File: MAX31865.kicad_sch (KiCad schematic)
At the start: 22 parts, among them J1 connector, J2 Screw_Terminal_01x04, U1 MAX31865, U2 MIC5225

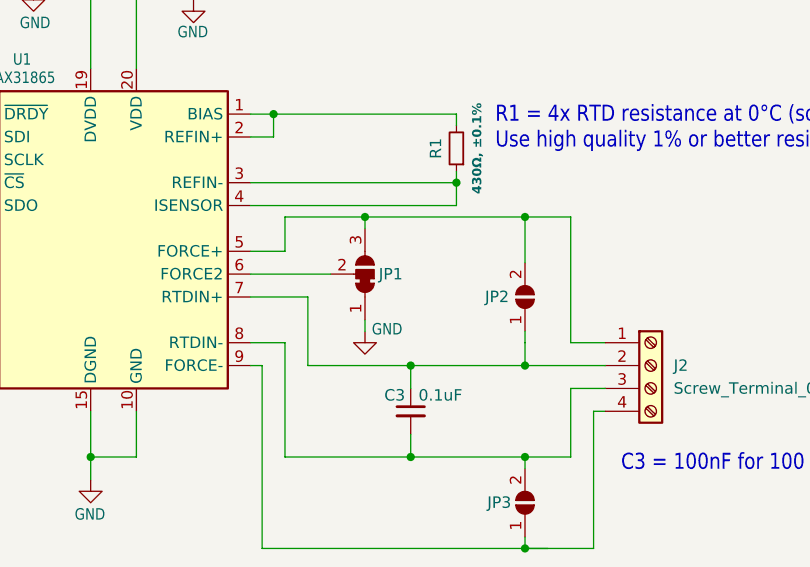
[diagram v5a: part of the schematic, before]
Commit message: schematic update
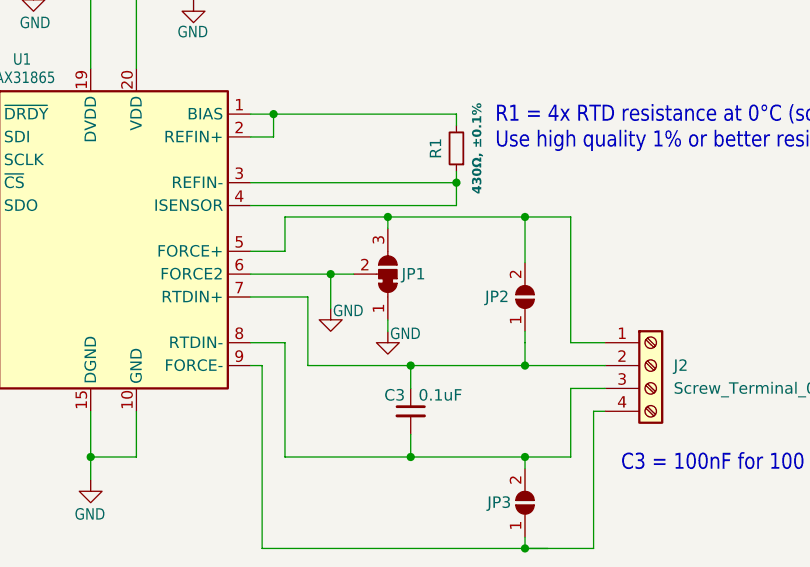
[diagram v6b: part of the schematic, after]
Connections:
- net GND: now also JP1.2 (C), U1.6 (FORCE2)
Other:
- moved on the sheet: JP1
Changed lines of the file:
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@@
 	)
 	(junction
+		(at 153.67 99.06)
+		(diameter 0)
+		(color 0 0 0 0)
+	)
+	(junction
 		(at 175.26 119.38)
 		(diameter 0)
@@
 	)
 	(junction
-		(at 157.48 92.71)
+		(at 127 119.38)
 		(diameter 0)
 		(color 0 0 0 0)
 	)
 	(junction
-		(at 127 119.38)
+		(at 68.58 113.03)
 		(diameter 0)
 		(color 0 0 0 0)
 	)
 	(junction
-		(at 68.58 113.03)
+		(at 160.02 92.71)
 		(diameter 0)
 		(color 0 0 0 0)
@@
 	(wire
 		(pts
-			(xy 157.48 92.71) (xy 175.26 92.71)
-		)
-		(stroke
-			(width 0.1524)
-			(type solid)
-		)
-	)
-	(wire
-		(pts
 			(xy 132.08 59.69) (xy 132.08 76.2)
 		)
@@
 	(wire
 		(pts
-			(xy 148.59 92.71) (xy 157.48 92.71)
+			(xy 148.59 92.71) (xy 160.02 92.71)
 		)
 		(stroke
@@
 	(wire
 		(pts
+			(xy 153.67 99.06) (xy 156.21 99.06)
+		)
+		(stroke
+			(width 0.1524)
+			(type solid)
+		)
+	)
+	(wire
+		(pts
 			(xy 175.26 109.22) (xy 184.15 109.22)
 		)
@@
 	(wire
 		(pts
-			(xy 157.48 92.71) (xy 157.48 93.98)
+			(xy 160.02 92.71) (xy 160.02 93.98)
 		)
 		(stroke
@@
 	(wire
 		(pts
+			(xy 160.02 92.71) (xy 175.26 92.71)
+		)
+		(stroke
+			(width 0.1524)
+			(type solid)
+		)
+	)
+	(wire
+		(pts
 			(xy 114.3 86.36) (xy 91.44 86.36)
 		)
@@
 	(wire
 		(pts
+			(xy 153.67 99.06) (xy 153.67 102.87)
+		)
+		(stroke
+			(width 0)
+			(type default)
+		)
+	)
+	(wire
+		(pts
 			(xy 138.43 67.31) (xy 138.43 68.58)
 		)
@@
 	(wire
 		(pts
-			(xy 157.48 105.41) (xy 157.48 104.14)
+			(xy 160.02 105.41) (xy 160.02 104.14)
 		)
 		(stroke
@@
 	(symbol
 		(lib_id "power:GND")
+		(at 153.67 102.87 0)
+		(unit 1)
+		(exclude_from_sim no)
+		(in_bom yes)
+		(on_board yes)
+		(dnp no)
+		(property "Reference" "#U$08"
+			(at 153.67 102.87 0)
+			(effects
+				(font
+					(size 1.27 1.27)
+				)
+				(hide yes)
+			)
+		)
+		(property "Value" "GND"
+			(at 153.924 103.886 0)
+			(effects
+				(font
+					(size 1.27 1.0795)
+				)
+				(justify left bottom)
+			)
+		)
+		(property "Footprint" ""
+			(at 153.67 102.87 0)
+			(effects
+				(font
+					(size 1.27 1.27)
+				)
+				(hide yes)
+			)
+		)
+		(property "Datasheet" ""
+			(at 153.67 102.87 0)
+			(effects
+				(font
+					(size 1.27 1.27)
+				)
+				(hide yes)
+			)
+		)
+		(property "Description" "Power symbol creates a global label with name \"GND\" , ground"
+			(at 153.67 102.87 0)
+			(effects
+				(font
+					(size 1.27 1.27)
+				)
+				(hide yes)
+			)
+		)
+		(pin "1"
+		)
+		(instances
+			(project "MAX31865"
+				(path "/7d3dfe06-ad22-4135-8721-3b06d69e4560"
+					(reference "#U$08")
+					(unit 1)
+				)
+			)
+		)
+	)
+	(symbol
+		(lib_id "power:GND")
 		(at 91.44 130.81 0)
 		(unit 1)
@@
 	(symbol
 		(lib_id "power:GND")
-		(at 157.48 105.41 0)
+		(at 160.02 105.41 0)
 		(unit 1)
 		(exclude_from_sim no)
@@
 		(dnp no)
 		(property "Reference" "#U$06"
-			(at 157.48 105.41 0)
+			(at 160.02 105.41 0)
 			(effects
 				(font
@@
 		)
 		(property "Value" "GND"
-			(at 158.242 105.918 0)
+			(at 160.274 106.426 0)
 			(effects
 				(font
@@
 		)
 		(property "Footprint" ""
-			(at 157.48 105.41 0)
+			(at 160.02 105.41 0)
 			(effects
 				(font
@@
 		)
 		(property "Datasheet" ""
-			(at 157.48 105.41 0)
+			(at 160.02 105.41 0)
 			(effects
 				(font
@@
 		)
 		(property "Description" "Power symbol creates a global label with name \"GND\" , ground"
-			(at 157.48 105.41 0)
+			(at 160.02 105.41 0)
 			(effects
 				(font
@@
 	(symbol
 		(lib_id "Jumper:SolderJumper_3_Bridged12")
-		(at 157.48 99.06 270)
+		(at 160.02 99.06 270)
 		(mirror x)
 		(unit 1)
@@
 		(dnp no)
 		(property "Reference" "JP1"
-			(at 159.004 99.06 90)
+			(at 161.544 99.06 90)
 			(effects
 				(font
@@
 		)
 		(property "Value" "SolderJumper_3_Bridged12"
-			(at 160.02 97.7901 90)
+			(at 162.56 97.7901 90)
 			(effects
 				(font
@@
 		)
 		(property "Footprint" "Jumper:SolderJumper-3_P1.3mm_Bridged12_Pad1.0x1.5mm"
-			(at 157.48 99.06 0)
+			(at 160.02 99.06 0)
 			(effects
 				(font
@@
 		)
 		(property "Datasheet" "~"
-			(at 157.48 99.06 0)
+			(at 160.02 99.06 0)
 			(effects
 				(font
@@
 		)
 		(property "Description" "3-pole Solder Jumper, pins 1+2 closed/bridged"
-			(at 157.48 99.06 0)
+			(at 160.02 99.06 0)
 			(effects
 				(font

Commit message: implemented Eurocircuits design remarks
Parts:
- FB1: footprint Inductor_SMD:L_0805_2012Metric -> external_footprints:LI0805G201R-10
- J2: MPN 0393570004 -> 039357-0004
- U1: footprint Package_DFN_QFN:TQFN-20-1EP_5x5mm_P0.65mm_EP3.25x3.25mm -> external_footprints:MAX31865ATP+
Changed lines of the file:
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@@
 			)
 		)
-		(property "Datasheet" "~"
+		(property "Datasheet" ""
 			(at 91.44 123.19 0)
 			(effects
@@
 			)
 		)
-		(property "Datasheet" "~"
+		(property "Datasheet" ""
 			(at 175.26 124.46 0)
 			(effects
@@
 			)
 		)
-		(property "Datasheet" "~"
+		(property "Datasheet" ""
 			(at 175.26 101.6 0)
 			(effects
@@
 			)
 		)
-		(property "Datasheet" "~"
+		(property "Datasheet" ""
 			(at 99.06 76.2 0)
 			(effects
@@
 			)
 		)
-		(property "Datasheet" "~"
+		(property "Datasheet" ""
 			(at 60.96 52.07 0)
 			(effects
@@
 			)
 		)
-		(property "Footprint" "Package_DFN_QFN:TQFN-20-1EP_5x5mm_P0.65mm_EP3.25x3.25mm"
+		(property "Footprint" "external_footprints:MAX31865ATP+"
 			(at 133.35 113.03 0)
 			(effects
@@
 			)
 		)
-		(property "Datasheet" "https://datasheets.maximintegrated.com/en/ds/MAX31865.pdf"
+		(property "Datasheet" ""
 			(at 129.54 88.9 0)
 			(effects
@@
 			)
 		)
-		(property "Datasheet" "~"
+		(property "Datasheet" ""
 			(at 73.66 90.17 0)
 			(effects
@@
 			)
 		)
-		(property "Datasheet" "~"
+		(property "Datasheet" ""
 			(at 167.64 85.09 0)
 			(effects
@@
 			)
 		)
-		(property "Datasheet" "~"
+		(property "Datasheet" ""
 			(at 138.43 64.77 0)
 			(effects
@@
 			)
 		)
-		(property "Footprint" "Inductor_SMD:L_0805_2012Metric"
+		(property "Footprint" "external_footprints:LI0805G201R-10"
 			(at 133.858 55.88 90)
 			(effects
@@
 			)
 		)
-		(property "Datasheet" "~"
+		(property "Datasheet" ""
 			(at 132.08 55.88 0)
 			(effects
@@
 			)
 		)
-		(property "Datasheet" "~"
+		(property "Datasheet" ""
 			(at 162.56 114.3 0)
 			(effects
@@
 			)
 		)
-		(property "Datasheet" "~"
+		(property "Datasheet" ""
 			(at 134.62 157.48 0)
 			(effects
@@
 			)
 		)
-		(property "Datasheet" "~"
+		(property "Datasheet" ""
 			(at 120.65 63.5 0)
 			(effects
@@
 			)
 		)
-		(property "Datasheet" "~"
+		(property "Datasheet" ""
 			(at 189.23 109.22 0)
 			(effects
@@
 			)
 		)
-		(property "MPN" "0393570004"
+		(property "MPN" "039357-0004"
 			(at 189.23 109.22 0)
 			(effects
@@
 			)
 		)
-		(property "Datasheet" "~"
+		(property "Datasheet" ""
 			(at 53.34 52.07 0)
 			(effects
@@
 			)
 		)
-		(property "Datasheet" "~"
+		(property "Datasheet" ""
 			(at 95.25 69.85 0)
 			(effects
@@
 			)
 		)
-		(property "Datasheet" "~"
+		(property "Datasheet" ""
 			(at 63.5 120.65 0)
 			(effects
@@
 			)
 		)
-		(property "Datasheet" "~"
+		(property "Datasheet" ""
 			(at 160.02 99.06 0)
 			(effects
@@
 			)
 		)
-		(property "Datasheet" "~"
+		(property "Datasheet" ""
 			(at 91.44 76.2 0)
 			(effects
@@
 			)
 		)
-		(property "Datasheet" "~"
+		(property "Datasheet" ""
 			(at 73.66 86.36 0)
 			(effects

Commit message: BOM presets update
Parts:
- C4, C5: Component package type C_0805 -> (none)
- D1, D2, D3: Component package type SOD-323 -> (none)
- J1: Component package type / -> (none)
- U1: Component package type 20-TQFN (5x5) -> (none)
- U2: Component package type SOT-235 -> (none)
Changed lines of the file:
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@@
 			)
 		)
-		(property "Component package type" "SOT-235"
-			(at 73.66 119.38 0)
-			(effects
-				(font
-					(size 1.27 1.27)
-				)
-				(hide yes)
-			)
-		)
 		(property "MPN" "MIC5225-3.3YM5-TR"
 			(at 73.66 119.38 0)
@@
 			)
 		)
-		(property "Component package type" "C_0805"
-			(at 91.44 123.19 0)
-			(effects
-				(font
-					(size 1.27 1.27)
-				)
-				(hide yes)
-			)
-		)
 		(property "MPN" "/"
 			(at 91.44 123.19 0)
@@
 			)
 		)
-		(property "Component package type" ""
-			(at 175.26 124.46 0)
-			(effects
-				(font
-					(size 1.27 1.27)
-				)
-				(hide yes)
-			)
-		)
 		(property "MPN" ""
 			(at 175.26 124.46 0)
@@
 			)
 		)
-		(property "Component package type" ""
-			(at 175.26 101.6 0)
-			(effects
-				(font
-					(size 1.27 1.27)
-				)
-				(hide yes)
-			)
-		)
 		(property "MPN" ""
 			(at 175.26 101.6 0)
@@
 			)
 		)
-		(property "Component package type" ""
-			(at 99.06 76.2 0)
-			(effects
-				(font
-					(size 1.27 1.27)
-				)
-				(hide yes)
-			)
-		)
 		(property "MPN" "/"
 			(at 99.06 76.2 0)
@@
 			)
 		)
-		(property "Component package type" ""
-			(at 60.96 52.07 0)
-			(effects
-				(font
-					(size 1.27 1.27)
-				)
-				(hide yes)
-			)
-		)
 		(property "MPN" ""
 			(at 60.96 52.07 0)
@@
 			)
 		)
-		(property "Component package type" "20-TQFN (5x5)"
-			(at 129.54 96.52 0)
-			(effects
-				(font
-					(size 1.27 1.27)
-				)
-				(hide yes)
-			)
-		)
 		(property "MPN" "MAX31865ATP+"
 			(at 129.54 96.52 0)
@@
 			)
 		)
-		(property "Component package type" "SOD-323"
-			(at 73.66 90.17 0)
-			(effects
-				(font
-					(size 1.27 1.27)
-				)
-				(hide yes)
-			)
-		)
 		(property "MPN" "1N4148WX-TP"
 			(at 73.66 90.17 0)
@@
 			)
 		)
-		(property "Component package type" ""
-			(at 167.64 85.09 0)
-			(effects
-				(font
-					(size 1.27 1.27)
-				)
-				(hide yes)
-			)
-		)
 		(property "MPN" "/"
 			(at 167.64 85.09 0)
@@
 			)
 		)
-		(property "Component package type" ""
-			(at 138.43 64.77 0)
-			(effects
-				(font
-					(size 1.27 1.27)
-				)
-				(hide yes)
-			)
-		)
 		(property "MPN" "/"
 			(at 138.43 64.77 0)
@@
 			)
 		)
-		(property "Component package type" ""
-			(at 132.08 55.88 0)
-			(effects
-				(font
-					(size 1.27 1.27)
-				)
-				(hide yes)
-			)
-		)
 		(property "MPN" "LI0805G201R-10"
 			(at 132.08 55.88 0)
@@
 			)
 		)
-		(property "Component package type" ""
-			(at 162.56 114.3 0)
-			(effects
-				(font
-					(size 1.27 1.27)
-				)
-				(hide yes)
-			)
-		)
 		(property "MPN" "/"
 			(at 162.56 114.3 0)
@@
 			)
 		)
-		(property "Component package type" "/"
-			(at 134.62 157.48 0)
-			(effects
-				(font
-					(size 1.27 1.27)
-				)
-				(hide yes)
-			)
-		)
 		(property "MPN" "TSW-108-09-G-S"
 			(at 134.62 157.48 0)
@@
 			)
 		)
-		(property "Component package type" ""
-			(at 120.65 63.5 0)
-			(effects
-				(font
-					(size 1.27 1.27)
-				)
-				(hide yes)
-			)
-		)
 		(property "MPN" "/"
 			(at 120.65 63.5 0)
@@
 			)
 		)
-		(property "Component package type" ""
-			(at 53.34 52.07 0)
-			(effects
-				(font
-					(size 1.27 1.27)
-				)
-				(hide yes)
-			)
-		)
 		(property "MPN" ""
 			(at 53.34 52.07 0)
@@
 			)
 		)
-		(property "Component package type" ""
-			(at 95.25 69.85 0)
-			(effects
-				(font
-					(size 1.27 1.27)
-				)
-				(hide yes)
-			)
-		)
 		(property "MPN" "/"
 			(at 95.25 69.85 0)
@@
 			)
 		)
-		(property "Component package type" "C_0805"
-			(at 63.5 120.65 0)
-			(effects
-				(font
-					(size 1.27 1.27)
-				)
-				(hide yes)
-			)
-		)
 		(property "MPN" "/"
 			(at 63.5 120.65 0)
@@
 			)
 		)
-		(property "Component package type" ""
-			(at 91.44 76.2 0)
-			(effects
-				(font
-					(size 1.27 1.27)
-				)
-				(hide yes)
-			)
-		)
 		(property "MPN" "/"
 			(at 91.44 76.2 0)
@@
 			)
 		)
-		(property "Component package type" "SOD-323"
-			(at 73.66 86.36 0)
-			(effects
-				(font
-					(size 1.27 1.27)
-				)
-				(hide yes)
-			)
-		)
 		(property "MPN" "1N4148WX-TP"
 			(at 73.66 86.36 0)
@@
 			(at 73.66 82.55 0)
 			(effects
-				(font
-					(size 1.27 1.27)
-				)
-				(hide yes)
-			)
-		)
-		(property "Component package type" "SOD-323"
-			(at 73.66 82.55 0)
-			(effects
